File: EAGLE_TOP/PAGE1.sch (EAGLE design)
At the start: 101 parts, among them Q1 IRF640, U1 NE555_SOP8, U10 NE556_SOP14, U11 4017_SOP16, U12 4017_SOP16, U13 4518_SMD, U14 4510_DIP, U15 4001_SOP14, U16 4081, U2 4040, U3 4030, U4 4030, U5 LM324, U6 4081_SMD, U7 4017_SOP16, U8 4013_SMD, U9 4013_SMD

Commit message: top PCB completed
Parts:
- removed C11, C15, C16, C19, C2, C20, C21, C22, C23, C24, C25, C26, C27, C5, C6, C7, C8, C9: 0.1uF, !JKS:CAP_NP_SMD2012
- removed C12, C13, C14, C17, C18, C3: 10uF, !JKS:CAP_POL_NOR
- removed C4: 0.012uF, !JKS:CAP_POL_NOR
- removed D1, D10, D11, D12, D13, D14, D15, D16, D2, D3, D4, D5, D6, D7, D8, D9: 1N4148, !JKS:DIODE_SMD
- removed LED1, LED2, LED3, LED4: (no value), !JKS:LED_BEN
- removed P1: (no value), !JKS:POWER_2
- removed R11, R12, R14, R15, R39, R41, R43, R45, R46, R47: 20K, !JKS:RES_2012
- removed R13, R16, R34, R36, R38, R40, R42, R44, R48: 10K, !JKS:RES_2012
- removed R18: 1K, !JKS:RES_2012
- removed R19, R20, R21: 100k, !JKS:RES_2012
- removed R35, R37: 2.2K, !JKS:RES_2012
- removed U1: NE555_SOP8, !JKS:NE555_SOP8
- removed U10: NE556_SOP14, !JKS:NE556_SOP14
- removed U11, U12, U7: 4017_SOP16, !JKS:4017_SOP16
- removed U13: 4518_SMD, !JKS:4518_SMD
- removed U14: 4510_DIP, !JKS:4510_DIP
- removed U15: 4001_SOP14, !JKS:4001_SOP14
- removed U16: 4081, !JKS:4081
- removed U2: 4040, !JKS:4040
- removed U3, U4: 4030, !JKS:4030
- removed U5: LM324, !JKS:LM324
- removed U6: 4081_SMD, !JKS:4081_SMD
- removed U8, U9: 4013_SMD, !SEM_03:4013_SMD
- removed VR1: 10K, !JKS:VR_BIG
- added CON1: TREE_CON, !JKS:TREE_CON
- added Q2, Q3: C1815, !JKS:NPN
- added Q4, Q5, Q6: IRF640, transistor-fet:IRF620
- added SW1: (no value), !JKS:PUSH_SW
- C1: value 0.1uF -> 47pF; device !JKS:CAP_POL_NOR -> !JKS:CAP_NP_SMD2012
- Q1: value IRF640 -> C1815; device transistor-fet:IRF620 -> !JKS:NPN
- R10, R8: value 10K -> 1K
- R2: value 1K -> 470k
- R3: value 20K -> 470k
- R4: value 10K -> 470k
- R5: value 20K -> 330
- R6: value 10K -> 220
- R7: value 20K -> 220
- R9: value 20K -> 1K
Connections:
- removed net FASTER_CV: R44.2, R45.2, R47.2, U10B.CV
- removed net MOD_BREATH: IDC1.10, LED1.P$1, U6A.P$1, U7G$1.Q0
- removed net MOD_FAST3: IDC1.12, LED2.P$1, U15A.IN1, U15A.IN2, U7G$1.Q1
- removed net MOD_FASTER: C20.1, IDC1.14, LED3.P$1, U15C.IN1, U15C.IN2, U7G$1.Q2
- removed net MOD_STATIC: D10.1, D11.1, D9.1, IDC1.16, LED4.P$1, U7G$1.Q3
- removed net N$1: D1.1, VR1.1
- removed net N$10: U2G$1.Q9, U3C.IN1
- removed net N$11: U2G$1.Q10, U3D.IN1
- removed net N$12: U2G$1.Q11, U4A.IN1
- removed net N$14: R3.1, U3A.OUT
- removed net N$15: R5.1, U3B.OUT
- removed net N$16: R7.1, U3C.OUT
- removed net N$17: R9.1, U3D.OUT
- removed net N$18: R11.1, U4A.OUT
- removed net N$19: R12.1, R3.2, R4.1
- removed net N$2: R1.2, U1.DIS, VR1.2
- removed net N$20: R4.2, R5.2, R6.1
- removed net N$21: R6.2, R7.2, R8.1
- removed net N$22: R10.1, R8.2, R9.2
- removed net N$23: R10.2, R11.2, R13.1
- removed net N$24: C3.1, R13.2, U5A.+
- removed net N$25: R14.1, U5A.-, U5A.OUT
- removed net N$26: R15.2, R16.2, U5B.OUT, U6A.P$2
- removed net N$27: R14.2, R15.1, U5B.+
- removed net N$28: C4.1, R16.1, U5B.-
- removed net N$29: D3.1, D4.1, D5.1, U6A.P$3
- removed net N$3: D2.2, VR1.3
- removed net N$32: U7G$1.MR, U7G$1.Q4
- removed net N$33: LED1.P$2, LED2.P$2, LED3.P$2, LED4.P$2, R18.1
- removed net N$34: U6B.P$2, U8A.!Q
- removed net N$35: U6B.P$1, U8B.!Q
- removed net N$36: U6B.P$3, U8A.D
- removed net N$37: R19.1, U8A.Q, U8B.D
- removed net N$38: R20.1, U8B.Q, U9A.D
- removed net N$39: U2G$1.Q12, U3A.IN2, U3B.IN2, U3C.IN2, U3D.IN2, U4A.IN2, U8A.CLK, U8B.CLK, U9A.CLK
- removed net N$4: C2.1, U1.CV
- removed net N$40: R21.1, U9A.Q
- removed net N$5: C1.1, D1.2, D2.1, U1.THR, U1.TRG
- removed net N$58: C17.1, R35.2, U10A.THR, U10A.TRG
- removed net N$59: R34.2, R35.1, U10A.DIS
- removed net N$6: R2.1, U1.OUT, U2G$1.!CLK
- removed net N$60: U10A.OUT, U11G$1.CLK
- removed net N$61: C19.1, U10A.CV
- removed net N$62: U13A.MR, U13A.Q2
- removed net N$63: U11G$1.!CO, U13A.E
- removed net N$64: U11G$1.MR, U15A.OUT
- removed net N$65: U13A.Q0, U15B.IN1
- removed net N$66: U13A.Q1, U15B.IN2
- removed net N$67: U11G$1.Q1, U16A.P$1
- removed net N$68: U11G$1.Q2, U16B.P$2
- removed net N$69: U11G$1.Q3, U16C.P$1
- removed net N$7: Q1.G, R2.2
- removed net N$70: U15B.OUT, U16A.P$2, U16B.P$1, U16C.P$2
- removed net N$71: D6.1, U16A.P$3
- removed net N$72: D7.1, U16B.P$3
- removed net N$73: D8.1, U16C.P$3
- removed net N$74: R36.2, R37.1, U10B.DIS
- removed net N$75: C18.1, R37.2, U10B.THR, U10B.TRG
- removed net N$76: C20.2, R48.1, U14.PE
- removed net N$77: U10B.OUT, U12G$1.CLK
- removed net N$78: D12.2, D13.2, U12G$1.MR
- removed net N$79: R39.1, U14.Q1
- removed net N$8: U2G$1.Q7, U3A.IN1
- removed net N$80: D12.1, U15C.OUT
- removed net N$81: D14.1, U12G$1.Q1
- removed net N$82: D15.1, U12G$1.Q2
- removed net N$83: D16.1, U12G$1.Q3
- removed net N$84: C25.1, D13.1, R38.1
- removed net N$85: U13B.MR, U13B.Q2
- removed net N$86: R38.2, U12G$1.Q4, U13B.CLK
- removed net N$87: R41.1, U14.Q2
- removed net N$88: R43.1, U14.Q3
- removed net N$89: U13B.Q1, U14.CLK
- removed net N$9: U2G$1.Q8, U3B.IN1
- removed net N$90: R45.1, U14.Q4
- removed net N$91: R39.2, R40.1, R46.1
- removed net N$92: R40.2, R41.2, R42.1
- removed net N$93: R42.2, R43.2, R44.1
- new net LED_ARR1: CON1.5, Q4.D
- new net LED_ARR2: CON1.6, Q5.D
- new net LED_ARR3: CON1.7, Q6.D
- new net N$13: Q4.G, R8.2
- new net N$43: Q5.G, R9.2
- new net N$46: Q6.G, R10.2
- new net N$50: Q1.B, R2.2
- new net N$53: Q2.B, R3.2
- new net N$54: Q3.B, R4.2
- new net N$55: Q1.C, R5.2
- new net N$56: Q2.C, R6.2
- new net N$57: Q3.C, R7.2
- new net RGB_B: CON1.4, R7.1
- new net RGB_G: CON1.3, R6.1
- new net RGB_R: CON1.2, R5.1
- net +5V: now also CON1.1; no longer C11.1, C15.1, C16.1, C21.1, C22.1, C23.1, C24.1, C26.1, C27.1, C5.1, C6.1, C7.1, C8.1, C9.1, P1.+, R34.1, R36.1, R47.1, U1.RST, U1.VCC, U10A.RST, U10B.RST, U10G$1.+, U11G$2.+, U12G$2.+, U13B.E, U13G$1.+, U14.A1, U14.A4, U14.VDD, U15G$1.+, U16G$5.+, U2G$2.+, U3G$5.+, U4G$5.+, U5G$1.+, U6G$5.+, U7G$2.+, U8G$3.VCC, U9G$3.VCC
- net GND: now also SW1.P$1; no longer C11.2, C12.2, C13.2, C14.2, C15.2, C16.2, C17.2, C18.2, C19.2, C2.2, C21.2, C22.2, C23.2, C24.2, C25.2, C26.2, C27.2, C3.2, C4.2, C5.2, C6.2, C7.2, C8.2, C9.2, P1.-, Q1.S, R12.2, R18.2, R46.2, R48.2, U1.GND, U10G$1.-, U11G$1.!EN, U11G$2.-, U12G$1.!EN, U12G$2.-, U13A.CLK, U13G$1.-, U14.A2, U14.A3, U14.CI, U14.GND, U14.MR, U14.U/!D, U15G$1.-, U16G$5.-, U2G$1.RST, U2G$2.-, U3G$5.-, U4G$5.-, U5G$1.-, U6G$5.-, U7G$1.!EN, U7G$2.-, U8A.R, U8A.S, U8B.R, U8B.S, U8G$3.GND, U9A.R, U9A.S, U9G$3.GND
- net LED_CON_1: now also R8.1; no longer D14.2, D3.2, D6.2, D9.2
- net LED_CON_2: now also R9.1; no longer D10.2, D15.2, D4.2, D7.2
- net LED_CON_3: now also Q5.S, R10.1; no longer D11.2, D16.2, D5.2, D8.2
- net LED_CON_B: now also R4.1; no longer C14.1, R21.2
- net LED_CON_G: now also R3.1; no longer C13.1, R20.2
- net LED_CON_R: now also R2.1; no longer C12.1, R19.2
- net MAIN_BRIGHT: now also Q1.E, Q2.E, Q3.E, Q4.S, Q6.S; no longer Q1.D
- net MOD_SW: now also C1.1, R1.2, SW1.P$2; no longer U7G$1.CLK

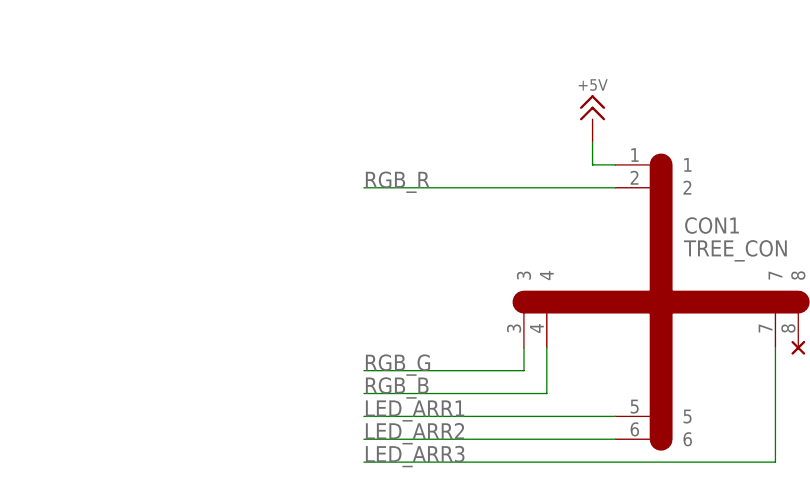
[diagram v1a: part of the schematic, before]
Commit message: Tree PCB Cmpl, top PCB Mdfi
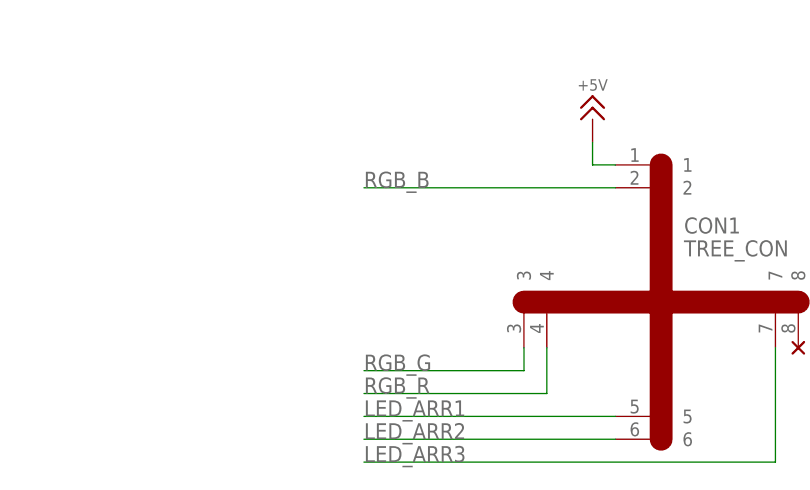
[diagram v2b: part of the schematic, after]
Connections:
- net RGB_B: now also CON1.2; no longer CON1.4
- net RGB_R: now also CON1.4; no longer CON1.2
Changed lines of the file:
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@@
 <grid distance="0.1" unitdist="inch" unit="inch" style="lines" multiple="1" display="yes" altdistance="0.01" altunitdist="inch" altunit="inch"/>
 <layers>
-<layer number="1" name="Top" color="4" fill="1" visible="yes" active="no"/>
-<layer number="2" name="Route2" color="16" fill="1" visible="yes" active="no"/>
-<layer number="3" name="Route3" color="17" fill="1" visible="yes" active="no"/>
-<layer number="4" name="Route4" color="18" fill="1" visible="yes" active="no"/>
-<layer number="5" name="Route5" color="19" fill="1" visible="yes" active="no"/>
-<layer number="6" name="Route6" color="25" fill="1" visible="yes" active="no"/>
-<layer number="7" name="Route7" color="26" fill="1" visible="yes" active="no"/>
-<layer number="8" name="Route8" color="27" fill="1" visible="yes" active="no"/>
-<layer number="9" name="Route9" color="28" fill="1" visible="yes" active="no"/>
-<layer number="10" name="Route10" color="29" fill="1" visible="yes" active="no"/>
-<layer number="11" name="Route11" color="30" fill="1" visible="yes" active="no"/>
-<layer number="12" name="Route12" color="20" fill="1" visible="yes" active="no"/>
-<layer number="13" name="Route13" color="21" fill="1" visible="yes" active="no"/>
-<layer number="14" name="Route14" color="22" fill="1" visible="yes" active="no"/>
-<layer number="15" name="Route15" color="23" fill="1" visible="yes" active="no"/>
-<layer number="16" name="Bottom" color="1" fill="1" visible="yes" active="no"/>
-<layer number="17" name="Pads" color="2" fill="1" visible="yes" active="no"/>
-<layer number="18" name="Vias" color="2" fill="1" visible="yes" active="no"/>
-<layer number="19" name="Unrouted" color="6" fill="1" visible="yes" active="no"/>
-<layer number="20" name="Dimension" color="24" fill="1" visible="yes" active="no"/>
-<layer number="21" name="tPlace" color="7" fill="1" visible="yes" active="no"/>
-<layer number="22" name="bPlace" color="7" fill="1" visible="yes" active="no"/>
-<layer number="23" name="tOrigins" color="15" fill="1" visible="yes" active="no"/>
-<layer number="24" name="bOrigins" color="15" fill="1" visible="yes" active="no"/>
-<layer number="25" name="tNames" color="7" fill="1" visible="yes" active="no"/>
-<layer number="26" name="bNames" color="7" fill="1" visible="yes" active="no"/>
-<layer number="27" name="tValues" color="7" fill="1" visible="yes" active="no"/>
-<layer number="28" name="bValues" color="7" fill="1" visible="yes" active="no"/>
+<layer number="1" name="Top" color="4" fill="1" visible="no" active="no"/>
+<layer number="2" name="Route2" color="16" fill="1" visible="no" active="no"/>
+<layer number="3" name="Route3" color="17" fill="1" visible="no" active="no"/>
+<layer number="4" name="Route4" color="18" fill="1" visible="no" active="no"/>
+<layer number="5" name="Route5" color="19" fill="1" visible="no" active="no"/>
+<layer number="6" name="Route6" color="25" fill="1" visible="no" active="no"/>
+<layer number="7" name="Route7" color="26" fill="1" visible="no" active="no"/>
+<layer number="8" name="Route8" color="27" fill="1" visible="no" active="no"/>
+<layer number="9" name="Route9" color="28" fill="1" visible="no" active="no"/>
+<layer number="10" name="Route10" color="29" fill="1" visible="no" active="no"/>
+<layer number="11" name="Route11" color="30" fill="1" visible="no" active="no"/>
+<layer number="12" name="Route12" color="20" fill="1" visible="no" active="no"/>
+<layer number="13" name="Route13" color="21" fill="1" visible="no" active="no"/>
+<layer number="14" name="Route14" color="22" fill="1" visible="no" active="no"/>
+<layer number="15" name="Route15" color="23" fill="1" visible="no" active="no"/>
+<layer number="16" name="Bottom" color="1" fill="1" visible="no" active="no"/>
+<layer number="17" name="Pads" color="2" fill="1" visible="no" active="no"/>
+<layer number="18" name="Vias" color="2" fill="1" visible="no" active="no"/>
+<layer number="19" name="Unrouted" color="6" fill="1" visible="no" active="no"/>
+<layer number="20" name="Dimension" color="24" fill="1" visible="no" active="no"/>
+<layer number="21" name="tPlace" color="7" fill="1" visible="no" active="no"/>
+<layer number="22" name="bPlace" color="7" fill="1" visible="no" active="no"/>
+<layer number="23" name="tOrigins" color="15" fill="1" visible="no" active="no"/>
+<layer number="24" name="bOrigins" color="15" fill="1" visible="no" active="no"/>
+<layer number="25" name="tNames" color="7" fill="1" visible="no" active="no"/>
+<layer number="26" name="bNames" color="7" fill="1" visible="no" active="no"/>
+<layer number="27" name="tValues" color="7" fill="1" visible="no" active="no"/>
+<layer number="28" name="bValues" color="7" fill="1" visible="no" active="no"/>
 <layer number="29" name="tStop" color="7" fill="3" visible="no" active="no"/>
 <layer number="30" name="bStop" color="7" fill="6" visible="no" active="no"/>
@@
 <layer number="35" name="tGlue" color="7" fill="4" visible="no" active="no"/>
 <layer number="36" name="bGlue" color="7" fill="5" visible="no" active="no"/>
-<layer number="37" name="tTest" color="7" fill="1" visible="yes" active="no"/>
-<layer number="38" name="bTest" color="7" fill="1" visible="yes" active="no"/>
+<layer number="37" name="tTest" color="7" fill="1" visible="no" active="no"/>
+<layer number="38" name="bTest" color="7" fill="1" visible="no" active="no"/>
 <layer number="39" name="tKeepout" color="4" fill="11" visible="no" active="no"/>
 <layer number="40" name="bKeepout" color="1" fill="11" visible="no" active="no"/>
@@
 <layer number="44" name="Drills" color="7" fill="1" visible="no" active="no"/>
 <layer number="45" name="Holes" color="7" fill="1" visible="no" active="no"/>
-<layer number="46" name="Milling" color="3" fill="1" visible="yes" active="no"/>
-<layer number="47" name="Measures" color="7" fill="1" visible="yes" active="no"/>
-<layer number="48" name="Document" color="7" fill="1" visible="yes" active="no"/>
-<layer number="49" name="Reference" color="7" fill="1" visible="yes" active="no"/>
-<layer number="50" name="dxf" color="7" fill="1" visible="yes" active="no"/>
-<layer number="51" name="tDocu" color="7" fill="1" visible="yes" active="no"/>
-<layer number="52" name="bDocu" color="7" fill="1" visible="yes" active="no"/>
-<layer number="53" name="tGND_GNDA" color="7" fill="9" visible="yes" active="no"/>
-<layer number="54" name="bGND_GNDA" color="1" fill="9" visible="yes" active="no"/>
-<layer number="56" name="wert" color="7" fill="1" visible="yes" active="no"/>
-<layer number="57" name="tCAD" color="7" fill="1" visible="yes" active="no"/>
-<layer number="59" name="tCarbon" color="7" fill="1" visible="yes" active="no"/>
-<layer number="60" name="bCarbon" color="7" fill="1" visible="yes" active="no"/>
+<layer number="46" name="Milling" color="3" fill="1" visible="no" active="no"/>
+<layer number="47" name="Measures" color="7" fill="1" visible="no" active="no"/>
+<layer number="48" name="Document" color="7" fill="1" visible="no" active="no"/>
+<layer number="49" name="Reference" color="7" fill="1" visible="no" active="no"/>
+<layer number="50" name="dxf" color="7" fill="1" visible="no" active="no"/>
+<layer number="51" name="tDocu" color="7" fill="1" visible="no" active="no"/>
+<layer number="52" name="bDocu" color="7" fill="1" visible="no" active="no"/>
+<layer number="53" name="tGND_GNDA" color="7" fill="9" visible="no" active="no"/>
+<layer number="54" name="bGND_GNDA" color="1" fill="9" visible="no" active="no"/>
+<layer number="56" name="wert" color="7" fill="1" visible="no" active="no"/>
+<layer number="57" name="tCAD" color="7" fill="1" visible="no" active="no"/>
+<layer number="59" name="tCarbon" color="7" fill="1" visible="no" active="no"/>
+<layer number="60" name="bCarbon" color="7" fill="1" visible="no" active="no"/>
 <layer number="88" name="SimResults" color="9" fill="1" visible="yes" active="yes"/>
 <layer number="89" name="SimProbes" color="9" fill="1" visible="yes" active="yes"/>
@@
 </segment>
 <segment>
-<wire x1="345.44" y1="106.68" x2="317.5" y2="106.68" width="0.1524" layer="91"/>
-<label x="317.5" y="106.68" size="1.778" layer="95"/>
-<pinref part="CON1" gate="G$1" pin="2"/>
+<wire x1="337.82" y1="88.9" x2="337.82" y2="83.82" width="0.1524" layer="91"/>
+<wire x1="337.82" y1="83.82" x2="317.5" y2="83.82" width="0.1524" layer="91"/>
+<label x="317.5" y="83.82" size="1.778" layer="95"/>
+<pinref part="CON1" gate="G$1" pin="4"/>
 </segment>
 </net>
@@
 </segment>
 <segment>
-<wire x1="337.82" y1="88.9" x2="337.82" y2="83.82" width="0.1524" layer="91"/>
-<wire x1="337.82" y1="83.82" x2="317.5" y2="83.82" width="0.1524" layer="91"/>
-<label x="317.5" y="83.82" size="1.778" layer="95"/>
-<pinref part="CON1" gate="G$1" pin="4"/>
-</segment>
-</net>
+<wire x1="345.44" y1="106.68" x2="317.5" y2="106.68" width="0.1524" layer="91"/>
+<label x="317.5" y="106.68" size="1.778" layer="95"/>
+<pinref part="CON1" gate="G$1" pin="2"/>
+</segment>
+</net>

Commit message: Operation Complete
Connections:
- new net N$1: Q1.E, Q2.E, Q3.E, Q4.S, Q5.S, Q6.S
- net LED_CON_3: no longer Q5.S
- net MAIN_BRIGHT: no longer Q1.E, Q2.E, Q3.E, Q4.S, Q6.S

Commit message: ver1 Complete
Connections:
- removed net N$1: Q1.E, Q2.E, Q3.E, Q4.S, Q5.S, Q6.S
- net MAIN_BRIGHT: now also Q1.E, Q2.E, Q3.E, Q4.S, Q5.S, Q6.S
